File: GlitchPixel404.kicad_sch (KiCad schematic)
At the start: 69 parts, among them J1 Barrel_Jack_Switch, J2 USB_C_Receptacle_USB2.0_16P, J3 Output, J4 VOLTLINK, J5 Conn_01x03, Q1 MMBT3904, Q2 AONR21357-ES, SW1 SW_SP3T, SW3 Reset, SW4 Boot, U1 74LVC2G34, U2 TPS54202DDC, U3 CH224K, U4 74LVC2G34, U5 HE2021A50HMR, U6 ESP32-PICO-MINI-02U-N8R2, U7 IRM-H6xxT

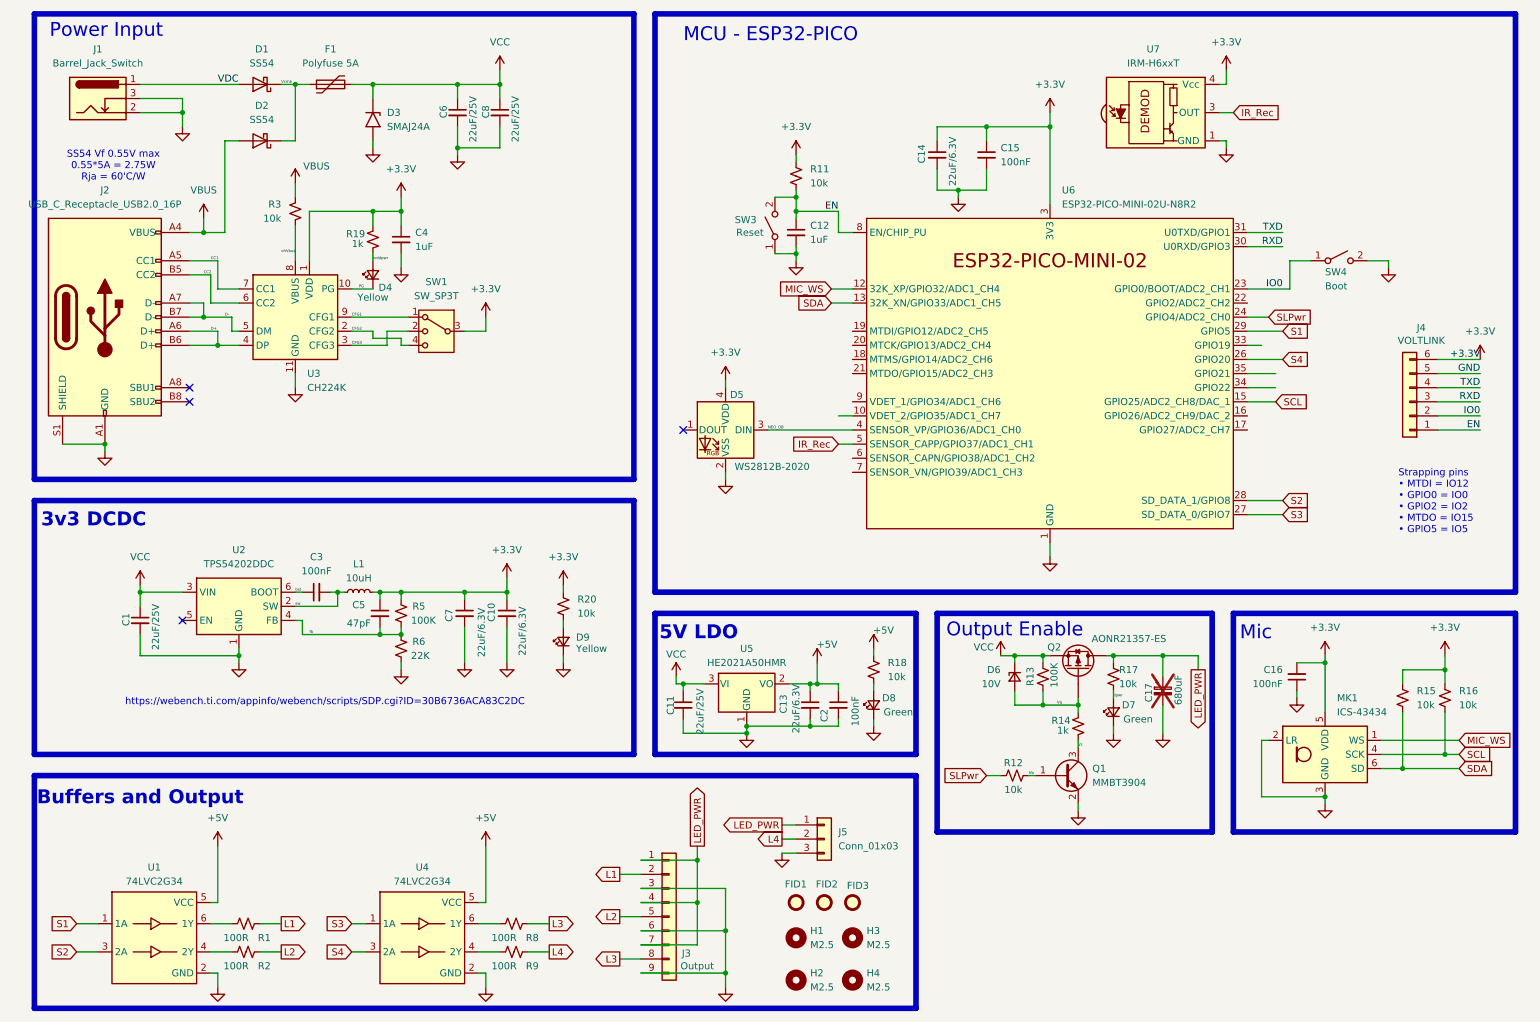
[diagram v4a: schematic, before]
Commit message: Adjusted component selection
Final silk and checks before prototype batch ready
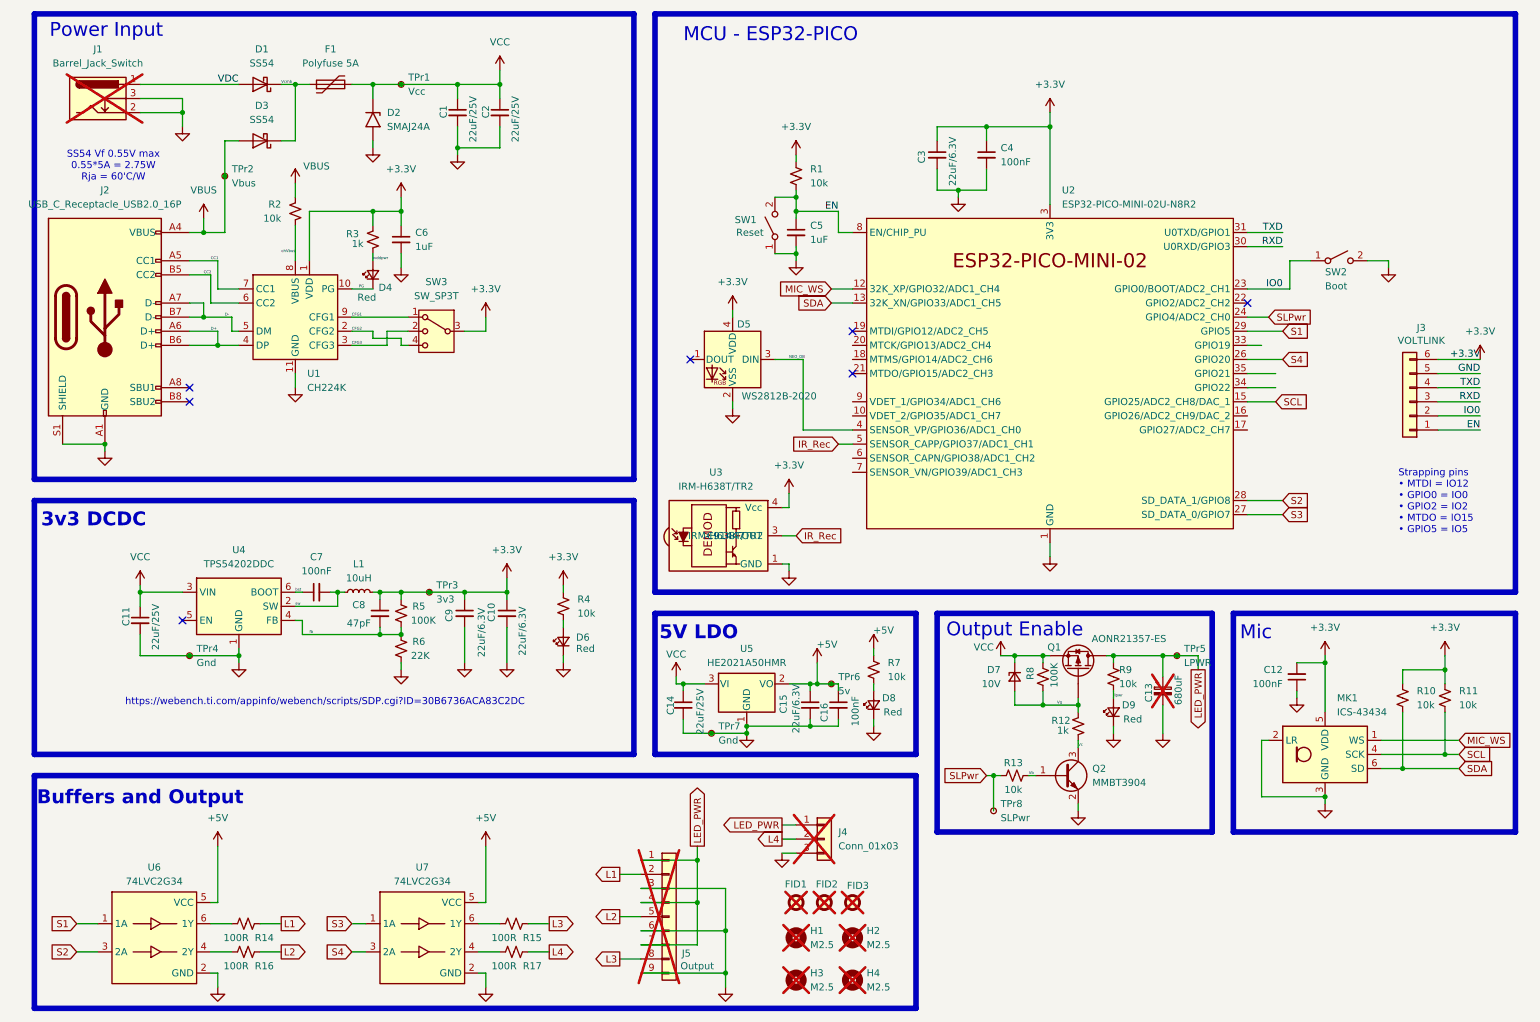
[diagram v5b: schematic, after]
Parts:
- added TPr1: Vcc, TestPoint:TestPoint_Pad_D1.0mm, symbol Connector:TestPoint_Small
- added TPr2: Vbus, TestPoint:TestPoint_Pad_D1.0mm, symbol Connector:TestPoint_Small
- added TPr3: 3v3, TestPoint:TestPoint_Pad_D1.0mm, symbol Connector:TestPoint_Small
- added TPr4, TPr7: Gnd, TestPoint:TestPoint_Pad_D1.0mm, symbol Connector:TestPoint_Small
- added TPr5: LPWR, TestPoint:TestPoint_Pad_D1.0mm, symbol Connector:TestPoint_Small
- added TPr6: 5v, TestPoint:TestPoint_Pad_D1.0mm, symbol Connector:TestPoint_Small
- added TPr8: SLPwr, TestPoint:TestPoint_Pad_D1.0mm, symbol Connector:TestPoint_Small
- D4: value Yellow -> Red; LCSC C72038 -> C2286
- D6: renamed from D9; value Yellow -> Red; LCSC C72038 -> C2286
- D8: value Green -> Red; LCSC C72043 -> C2286
- D9: renamed from D7; value Green -> Red; LCSC C72043 -> C2286
- FID1, FID2, FID3, H1, H4: now not fitted
- H2: renamed from H3; now not fitted
- H3: renamed from H2; now not fitted
- J1: now not fitted; now left out of the parts list
- J4: renamed from J5; now not fitted; now left out of the parts list
- J5: renamed from J3; now not fitted; now left out of the parts list
- SW1: renamed from SW3; LCSC C843663 -> C557591; MPN GT-TC029A-H020-L1A -> TS342A2P-WZ
- SW2: renamed from SW4; LCSC C843663 -> C557591; MPN GT-TC029A-H020-L1A -> TS342A2P-WZ
- U2: renamed from U6; LCSC C3013939 -> C2980306
- U3: renamed from U7; value IRM-H6xxT -> IRM-H638T/TR2; LCSC (none) -> C91447; MPN (none) -> IRM-H638T/TR2
- renumbered C6 to C1, C1 to C11, C16 to C12, C17 to C13, C11 to C14, C13 to C15, C2 to C16, C8 to C2, C14 to C3, C15 to C4, C12 to C5, C4 to C6, C3 to C7, C5 to C8, C7 to C9, D3 to D2, D2 to D3, D6 to D7, J4 to J3, Q2 to Q1, Q1 to Q2, R11 to R1, R15 to R10, R16 to R11, R14 to R12, R12 to R13, R1 to R14, R8 to R15, R2 to R16, R9 to R17, R3 to R2, R19 to R3, R20 to R4, R18 to R7, R13 to R8, R17 to R9, SW1 to SW3, U3 to U1, U2 to U4, U1 to U6, U4 to U7
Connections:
- net +3.3V: now also TPr3.1
- net +5V: now also TPr6.1
- net GND: now also TPr4.1, TPr7.1
- net LED_PWR: now also TPr5.1
- net SLPwr: now also TPr8.1
- net VBUS: now also TPr2.1
- net VCC: now also TPr1.1
- no-connect marks 4 -> 7
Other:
- moved on the sheet: D5, U3

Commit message: RevA1
Sent for manufacture of prototypes
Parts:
- added TPr10: Rx, TestPoint:TestPoint_Pad_D1.0mm, symbol Connector:TestPoint_Small
- added TPr9: Tx, TestPoint:TestPoint_Pad_D1.0mm, symbol Connector:TestPoint_Small
- J5: footprint Connector_PinSocket_2.54mm:PinSocket_1x09_P2.54mm_Vertical -> Inventel:CONN-TH_9P-P2.54_MX128-2.54-09P-GN01-CU-Y-A; LCSC (none) -> C5188449; now fitted; now in the parts list
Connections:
- net GND: now also J5.1 (Pin_1), J5.4 (Pin_4), J5.7 (Pin_7); no longer J5.3 (Pin_3), J5.6 (Pin_6), J5.9 (Pin_9)
- net L1: now also J5.8 (Pin_8); no longer J5.2 (Pin_2)
- net L3: now also J5.2 (Pin_2); no longer J5.8 (Pin_8)
- net LED_PWR: now also J5.3 (Pin_3), J5.6 (Pin_6), J5.9 (Pin_9); no longer J5.1 (Pin_1), J5.4 (Pin_4), J5.7 (Pin_7)
- net NEO_OB: now also U2.34 (GPIO22); no longer U2.4 (SENSOR_VP/GPIO36/ADC1_CH0)
- net RXD: now also TPr10.1
- net S1: now also U2.33 (GPIO19); no longer U2.29 (GPIO5)
- net S2: now also U2.16 (GPIO26/ADC2_CH9/DAC_2); no longer U2.28 (SD_DATA_1/GPIO8)
- net S3: now also U2.17 (GPIO27/ADC2_CH7); no longer U2.27 (SD_DATA_0/GPIO7)
- net TXD: now also TPr9.1
- net SCL renamed MIC_SCK
- net SDA renamed MIC_SDA
- no-connect marks 7 -> 18
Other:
- note added: ">= GPIO 34 are input only!"
- note added: "GPIO 6-11 dont show in WLED 15?"
- note added: "VoltLink"

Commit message: Add Drawings and 3D Files
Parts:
- J2: value USB_C_Receptacle_USB2.0_16P -> TYPE-C-31-M-12
- renumbered U2 to Ue
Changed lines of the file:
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@@
 			)
 		)
-		(property "Value" "USB_C_Receptacle_USB2.0_16P"
+		(property "Value" "TYPE-C-31-M-12"
 			(at 27.94 49.53 0)
 			(effects
@@
 		(dnp no)
 		(fields_autoplaced yes)
-		(property "Reference" "U2"
+		(property "Reference" "Ue"
 			(at 200.2633 46.99 0)
 			(effects
@@
 			(project ""
 				(path "/3cfb80c9-371d-4841-9148-eae536d7cb55"
-					(reference "U2")
+					(reference "Ue")
 					(unit 1)
 				)

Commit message: Started A2 HW Rev, Fixed R12
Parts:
- removed FID1, FID2, FID3: Fiducial, Fiducial:Fiducial_1mm_Mask2mm, symbol Mechanical:Fiducial
- R12: value 1k -> 10k; LCSC C11702 -> C25744
- renumbered Ue to Ue1
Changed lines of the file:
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@@
 	(title_block
 		(title "GlitchPixel404")
-		(date "2025-03-15")
-		(rev "A1")
+		(date "2025-07-17")
+		(rev "A2")
 		(company "Inventel")
 		(comment 1 "RBM")
@@
 	)
 	(symbol
-		(lib_id "Mechanical:Fiducial")
-		(at 162.56 175.26 0)
-		(unit 1)
-		(exclude_from_sim yes)
-		(in_bom no)
-		(on_board yes)
-		(dnp yes)
-		(property "Reference" "FID3"
-			(at 161.544 172.212 0)
-			(effects
-				(font
-					(size 1.27 1.27)
-				)
-				(justify left)
-			)
-		)
-		(property "Value" "Fiducial"
-			(at 165.1 176.5299 0)
-			(effects
-				(font
-					(size 1.27 1.27)
-				)
-				(justify left)
-				(hide yes)
-			)
-		)
-		(property "Footprint" "Fiducial:Fiducial_1mm_Mask2mm"
-			(at 162.56 175.26 0)
-			(effects
-				(font
-					(size 1.27 1.27)
-				)
-				(hide yes)
-			)
-		)
-		(property "Datasheet" "~"
-			(at 162.56 175.26 0)
-			(effects
-				(font
-					(size 1.27 1.27)
-				)
-				(hide yes)
-			)
-		)
-		(property "Description" "Fiducial Marker"
-			(at 162.56 175.26 0)
-			(effects
-				(font
-					(size 1.27 1.27)
-				)
-				(hide yes)
-			)
-		)
-		(instances
-			(project "GlitchPixel404"
-				(path "/3cfb80c9-371d-4841-9148-eae536d7cb55"
-					(reference "FID3")
-					(unit 1)
-				)
-			)
-		)
-	)
-	(symbol
-		(lib_id "Mechanical:Fiducial")
-		(at 152.4 175.26 0)
-		(unit 1)
-		(exclude_from_sim yes)
-		(in_bom no)
-		(on_board yes)
-		(dnp yes)
-		(property "Reference" "FID1"
-			(at 150.368 171.958 0)
-			(effects
-				(font
-					(size 1.27 1.27)
-				)
-				(justify left)
-			)
-		)
-		(property "Value" "Fiducial"
-			(at 154.94 176.5299 0)
-			(effects
-				(font
-					(size 1.27 1.27)
-				)
-				(justify left)
-				(hide yes)
-			)
-		)
-		(property "Footprint" "Fiducial:Fiducial_1mm_Mask2mm"
-			(at 152.4 175.26 0)
-			(effects
-				(font
-					(size 1.27 1.27)
-				)
-				(hide yes)
-			)
-		)
-		(property "Datasheet" "~"
-			(at 152.4 175.26 0)
-			(effects
-				(font
-					(size 1.27 1.27)
-				)
-				(hide yes)
-			)
-		)
-		(property "Description" "Fiducial Marker"
-			(at 152.4 175.26 0)
-			(effects
-				(font
-					(size 1.27 1.27)
-				)
-				(hide yes)
-			)
-		)
-		(instances
-			(project "GlitchPixel404"
-				(path "/3cfb80c9-371d-4841-9148-eae536d7cb55"
-					(reference "FID1")
-					(unit 1)
-				)
-			)
-		)
-	)
-	(symbol
 		(lib_id "power:GND")
 		(at 242.57 138.43 0)
@@
 	)
 	(symbol
-		(lib_id "Mechanical:Fiducial")
-		(at 157.48 175.26 0)
-		(unit 1)
-		(exclude_from_sim yes)
-		(in_bom no)
-		(on_board yes)
-		(dnp yes)
-		(property "Reference" "FID2"
-			(at 155.956 171.958 0)
-			(effects
-				(font
-					(size 1.27 1.27)
-				)
-				(justify left)
-			)
-		)
-		(property "Value" "Fiducial"
-			(at 160.02 176.5299 0)
-			(effects
-				(font
-					(size 1.27 1.27)
-				)
-				(justify left)
-				(hide yes)
-			)
-		)
-		(property "Footprint" "Fiducial:Fiducial_1mm_Mask2mm"
-			(at 157.48 175.26 0)
-			(effects
-				(font
-					(size 1.27 1.27)
-				)
-				(hide yes)
-			)
-		)
-		(property "Datasheet" "~"
-			(at 157.48 175.26 0)
-			(effects
-				(font
-					(size 1.27 1.27)
-				)
-				(hide yes)
-			)
-		)
-		(property "Description" "Fiducial Marker"
-			(at 157.48 175.26 0)
-			(effects
-				(font
-					(size 1.27 1.27)
-				)
-				(hide yes)
-			)
-		)
-		(instances
-			(project "GlitchPixel404"
-				(path "/3cfb80c9-371d-4841-9148-eae536d7cb55"
-					(reference "FID2")
-					(unit 1)
-				)
-			)
-		)
-	)
-	(symbol
 		(lib_id "Regulator_Linear:MCP1792x-5002xCB")
 		(at 143.51 135.89 0)
@@
 		(dnp no)
 		(fields_autoplaced yes)
-		(property "Reference" "Ue"
+		(property "Reference" "Ue1"
 			(at 200.2633 46.99 0)
 			(effects
@@
 			(project ""
 				(path "/3cfb80c9-371d-4841-9148-eae536d7cb55"
-					(reference "Ue")
+					(reference "Ue1")
 					(unit 1)
 				)
@@
 			)
 		)
-		(property "Value" "1k"
+		(property "Value" "10k"
 			(at 199.39 144.272 0)
 			(effects
@@
 			)
 		)
-		(property "LCSC" "C11702"
+		(property "LCSC" "C25744"
 			(at 203.2 143.51 0)
 			(effects
